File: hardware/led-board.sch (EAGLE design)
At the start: 22 parts, among them U1 ATMEGA168PA-AU

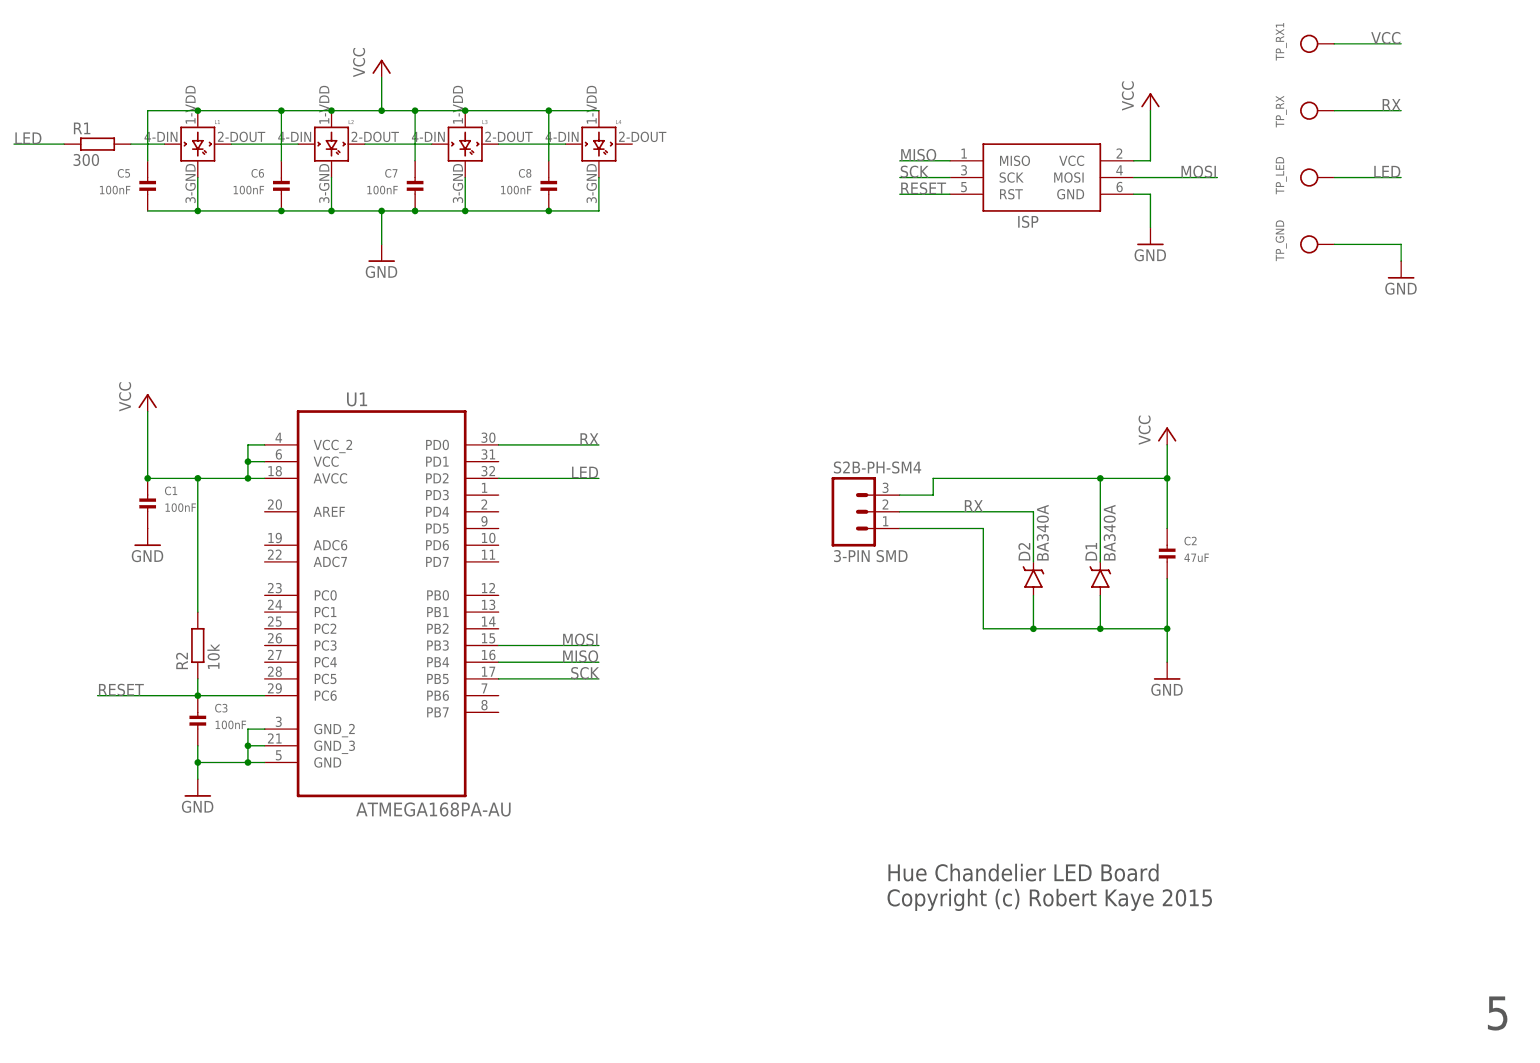
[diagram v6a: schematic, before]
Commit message: Changed L# -> D# for the LEDs
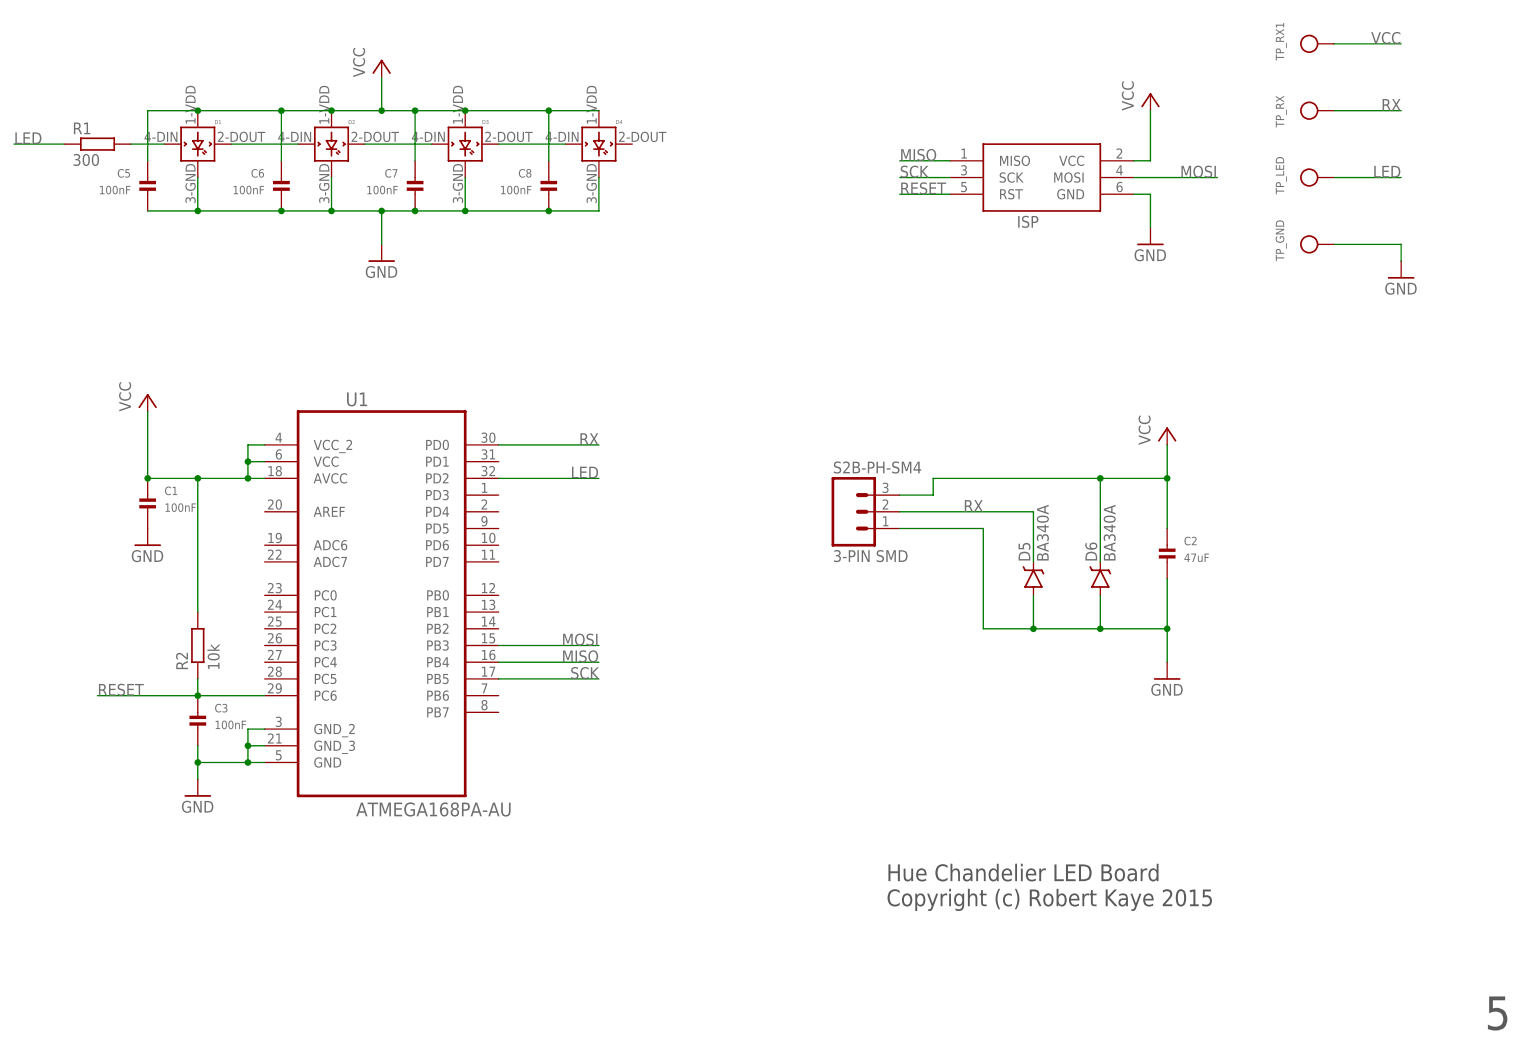
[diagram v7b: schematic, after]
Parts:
- removed L1, L2: WS2812B, adafruit:WS2812B
- added D5, D6: BA340A, SparkFun-DiscreteSemi:B340A
- D1, D2: value BA340A -> WS2812B; device SparkFun-DiscreteSemi:B340A -> adafruit:WS2812B; MPN B330A-13-F -> WS2812B; OC_NEWARK 12T1463 -> 43Y4720
- renumbered L3 to D3, L4 to D4
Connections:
- removed net N$5: D3.DIN, L2.DOUT
- new net D3: D2.DOUT, D3.DIN
- net GND: now also D1.GND, D2.GND, D5.A, D6.A; no longer D1.A, D2.A, L1.GND, L2.GND
- net N$2: now also D1.DOUT, D2.DIN; no longer L1.DOUT, L2.DIN
- net N$8: now also D1.DIN; no longer L1.DIN
- net RX: now also D5.C; no longer D2.C
- net VCC: now also D1.VDD, D2.VDD, D6.C; no longer D1.C, L1.VDD, L2.VDD
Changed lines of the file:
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@@
 </classes>
 <parts>
-<part name="L1" library="adafruit" deviceset="WS2812B" device="">
+<part name="D1" library="adafruit" deviceset="WS2812B" device="">
 <attribute name="MF" value=""/>
 <attribute name="MPN" value="WS2812B"/>
 <attribute name="OC_NEWARK" value="43Y4720"/>
 </part>
-<part name="L2" library="adafruit" deviceset="WS2812B" device="">
+<part name="D2" library="adafruit" deviceset="WS2812B" device="">
 <attribute name="MF" value=""/>
 <attribute name="MPN" value="WS2812B"/>
@@
 <attribute name="OC_NEWARK" value="68T2717"/>
 </part>
-<part name="L3" library="adafruit" deviceset="WS2812B" device="">
+<part name="D3" library="adafruit" deviceset="WS2812B" device="">
 <attribute name="MF" value=""/>
 <attribute name="MPN" value="WS2812B"/>
 <attribute name="OC_NEWARK" value="43Y4720"/>
 </part>
-<part name="L4" library="adafruit" deviceset="WS2812B" device="">
+<part name="D4" library="adafruit" deviceset="WS2812B" device="">
 <attribute name="MF" value=""/>
 <attribute name="MPN" value="WS2812B"/>
@@
 <attribute name="OC_NEWARK" value="68R4880"/>
 </part>
-<part name="D1" library="SparkFun-DiscreteSemi" deviceset="B340A" device="" value="BA340A">
+<part name="D6" library="SparkFun-DiscreteSemi" deviceset="B340A" device="" value="BA340A">
 <attribute name="MF" value=""/>
 <attribute name="MPN" value="B330A-13-F"/>
@@
 <attribute name="OC_NEWARK" value="unknown"/>
 </part>
-<part name="D2" library="SparkFun-DiscreteSemi" deviceset="B340A" device="" value="BA340A">
+<part name="D5" library="SparkFun-DiscreteSemi" deviceset="B340A" device="" value="BA340A">
 <attribute name="MF" value=""/>
 <attribute name="MPN" value="B330A-13-F"/>
@@
 </plain>
 <instances>
-<instance part="L1" gate="G$1" x="-38.1" y="93.98">
+<instance part="D1" gate="G$1" x="-38.1" y="93.98">
 <attribute name="OC_NEWARK" x="-38.1" y="93.98" size="1.778" layer="96" rot="MR0" display="off"/>
 <attribute name="MF" x="-38.1" y="93.98" size="1.778" layer="96" rot="MR0" display="off"/>
 <attribute name="MPN" x="-38.1" y="93.98" size="1.778" layer="96" rot="MR0" display="off"/>
 </instance>
-<instance part="L2" gate="G$1" x="-17.78" y="93.98">
+<instance part="D2" gate="G$1" x="-17.78" y="93.98">
 <attribute name="OC_NEWARK" x="-17.78" y="93.98" size="1.778" layer="96" rot="MR0" display="off"/>
 <attribute name="MF" x="-17.78" y="93.98" size="1.778" layer="96" rot="MR0" display="off"/>
@@
 <attribute name="MF" x="-10.16" y="27.94" size="1.778" layer="96" rot="MR0" display="off"/>
 </instance>
-<instance part="L3" gate="G$1" x="2.54" y="93.98">
+<instance part="D3" gate="G$1" x="2.54" y="93.98">
 <attribute name="OC_NEWARK" x="2.54" y="93.98" size="1.778" layer="96" rot="MR0" display="off"/>
 <attribute name="MF" x="2.54" y="93.98" size="1.778" layer="96" rot="MR0" display="off"/>
 <attribute name="MPN" x="2.54" y="93.98" size="1.778" layer="96" rot="MR0" display="off"/>
 </instance>
-<instance part="L4" gate="G$1" x="22.86" y="93.98">
+<instance part="D4" gate="G$1" x="22.86" y="93.98">
 <attribute name="OC_NEWARK" x="22.86" y="93.98" size="1.778" layer="96" rot="MR0" display="off"/>
 <attribute name="MF" x="22.86" y="93.98" size="1.778" layer="96" rot="MR0" display="off"/>
@@
 <attribute name="MPN" x="109.22" y="30.48" size="1.778" layer="96" rot="MR0" display="off"/>
 </instance>
-<instance part="D1" gate="G$1" x="99.06" y="27.94" rot="R90">
+<instance part="D6" gate="G$1" x="99.06" y="27.94" rot="R90">
 <attribute name="OC_NEWARK" x="99.06" y="27.94" size="1.778" layer="96" rot="MR0" display="off"/>
 <attribute name="MF" x="99.06" y="27.94" size="1.778" layer="96" rot="MR0" display="off"/>
@@
 <attribute name="MPN" x="134.62" y="99.06" size="1.778" layer="96" rot="MR0" display="off"/>
 </instance>
-<instance part="D2" gate="G$1" x="88.9" y="27.94" rot="R90">
+<instance part="D5" gate="G$1" x="88.9" y="27.94" rot="R90">
 <attribute name="OC_NEWARK" x="88.9" y="27.94" size="1.778" layer="96" rot="MR0" display="off"/>
 <attribute name="MF" x="88.9" y="27.94" size="1.778" layer="96" rot="MR0" display="off"/>
@@
 <wire x1="2.54" y1="83.82" x2="15.24" y2="83.82" width="0.1524" layer="91"/>
 <wire x1="15.24" y1="83.82" x2="22.86" y2="83.82" width="0.1524" layer="91"/>
-<pinref part="L4" gate="G$1" pin="GND"/>
+<pinref part="D4" gate="G$1" pin="GND"/>
 <wire x1="22.86" y1="88.9" x2="22.86" y2="83.82" width="0.1524" layer="91"/>
-<pinref part="L3" gate="G$1" pin="GND"/>
+<pinref part="D3" gate="G$1" pin="GND"/>
 <wire x1="2.54" y1="88.9" x2="2.54" y2="83.82" width="0.1524" layer="91"/>
-<pinref part="L2" gate="G$1" pin="GND"/>
+<pinref part="D2" gate="G$1" pin="GND"/>
 <wire x1="-17.78" y1="88.9" x2="-17.78" y2="83.82" width="0.1524" layer="91"/>
-<pinref part="L1" gate="G$1" pin="GND"/>
+<pinref part="D1" gate="G$1" pin="GND"/>
 <wire x1="-38.1" y1="88.9" x2="-38.1" y2="83.82" width="0.1524" layer="91"/>
 <junction x="-38.1" y="83.82"/>
@@
 <wire x1="109.22" y1="20.32" x2="109.22" y2="15.24" width="0.1524" layer="91"/>
 <junction x="109.22" y="20.32"/>
-<pinref part="D2" gate="G$1" pin="A"/>
+<pinref part="D5" gate="G$1" pin="A"/>
 <wire x1="88.9" y1="25.4" x2="88.9" y2="20.32" width="0.1524" layer="91"/>
-<pinref part="D1" gate="G$1" pin="A"/>
+<pinref part="D6" gate="G$1" pin="A"/>
 <wire x1="99.06" y1="25.4" x2="99.06" y2="20.32" width="0.1524" layer="91"/>
 <junction x="99.06" y="20.32"/>
@@
 <net name="N$2" class="0">
 <segment>
-<pinref part="L1" gate="G$1" pin="DOUT"/>
-<pinref part="L2" gate="G$1" pin="DIN"/>
+<pinref part="D1" gate="G$1" pin="DOUT"/>
+<pinref part="D2" gate="G$1" pin="DIN"/>
 <wire x1="-33.02" y1="93.98" x2="-22.86" y2="93.98" width="0.1524" layer="91"/>
 </segment>
@@
 <net name="N$1" class="0">
 <segment>
-<pinref part="L3" gate="G$1" pin="DOUT"/>
-<pinref part="L4" gate="G$1" pin="DIN"/>
+<pinref part="D3" gate="G$1" pin="DOUT"/>
+<pinref part="D4" gate="G$1" pin="DIN"/>
 <wire x1="7.62" y1="93.98" x2="17.78" y2="93.98" width="0.1524" layer="91"/>
 </segment>
@@
 </segment>
 </net>
-<net name="N$5" class="0">
-<segment>
-<pinref part="L2" gate="G$1" pin="DOUT"/>
-<pinref part="L3" gate="G$1" pin="DIN"/>
+<net name="D3" class="0">
+<segment>
+<pinref part="D2" gate="G$1" pin="DOUT"/>
+<pinref part="D3" gate="G$1" pin="DIN"/>
 <wire x1="-12.7" y1="93.98" x2="-2.54" y2="93.98" width="0.1524" layer="91"/>
 </segment>
@@
 <segment>
 <pinref part="R1" gate="G$1" pin="2"/>
-<pinref part="L1" gate="G$1" pin="DIN"/>
+<pinref part="D1" gate="G$1" pin="DIN"/>
 <wire x1="-48.26" y1="93.98" x2="-43.18" y2="93.98" width="0.1524" layer="91"/>
 </segment>
@@
 <segment>
 <wire x1="-45.72" y1="91.44" x2="-45.72" y2="99.06" width="0.1524" layer="91"/>
-<pinref part="L1" gate="G$1" pin="VDD"/>
+<pinref part="D1" gate="G$1" pin="VDD"/>
 <wire x1="-45.72" y1="99.06" x2="-38.1" y2="99.06" width="0.1524" layer="91"/>
-<pinref part="L2" gate="G$1" pin="VDD"/>
+<pinref part="D2" gate="G$1" pin="VDD"/>
 <wire x1="-38.1" y1="99.06" x2="-25.4" y2="99.06" width="0.1524" layer="91"/>
-<pinref part="L3" gate="G$1" pin="VDD"/>
+<pinref part="D3" gate="G$1" pin="VDD"/>
 <wire x1="-25.4" y1="99.06" x2="-17.78" y2="99.06" width="0.1524" layer="91"/>
 <wire x1="-17.78" y1="99.06" x2="-10.16" y2="99.06" width="0.1524" layer="91"/>
-<pinref part="L4" gate="G$1" pin="VDD"/>
+<pinref part="D4" gate="G$1" pin="VDD"/>
 <wire x1="-10.16" y1="99.06" x2="-5.08" y2="99.06" width="0.1524" layer="91"/>
 <wire x1="-5.08" y1="99.06" x2="2.54" y2="99.06" width="0.1524" layer="91"/>
@@
 <wire x1="109.22" y1="43.18" x2="109.22" y2="48.26" width="0.1524" layer="91"/>
 <junction x="109.22" y="43.18"/>
-<pinref part="D1" gate="G$1" pin="C"/>
+<pinref part="D6" gate="G$1" pin="C"/>
 <wire x1="99.06" y1="30.48" x2="99.06" y2="43.18" width="0.1524" layer="91"/>
 <junction x="99.06" y="43.18"/>
@@
 <wire x1="68.58" y1="38.1" x2="88.9" y2="38.1" width="0.1524" layer="91"/>
 <label x="81.28" y="38.1" size="1.778" layer="95" rot="MR0"/>
-<pinref part="D2" gate="G$1" pin="C"/>
+<pinref part="D5" gate="G$1" pin="C"/>
 <wire x1="88.9" y1="38.1" x2="88.9" y2="30.48" width="0.1524" layer="91"/>
 </segment>

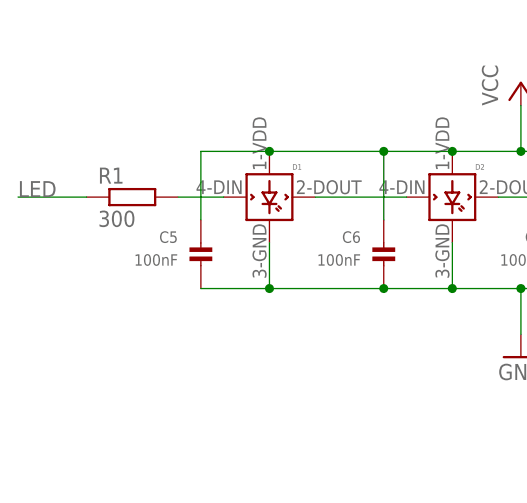
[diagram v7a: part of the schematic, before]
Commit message: Ported code to aduino and it looks like everything should fit!!!
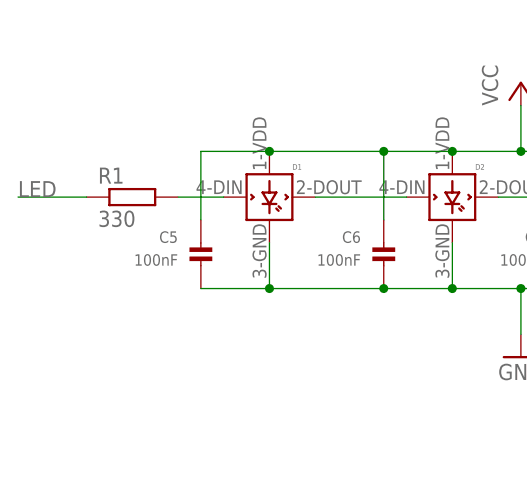
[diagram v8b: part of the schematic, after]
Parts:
- R1: value 300 -> 330; MF Multicomp Passives -> (none); MPN MC01W08051300R -> RC0805JR-07330RL; OC_NEWARK 58K4799 -> 66R3661
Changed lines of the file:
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@@
 <attribute name="OC_NEWARK" value="43Y4720"/>
 </part>
-<part name="R1" library="resistor" deviceset="R-EU_" device="R0805" value="300">
-<attribute name="MF" value="Multicomp Passives"/>
-<attribute name="MPN" value="MC01W08051300R"/>
-<attribute name="OC_NEWARK" value="58K4799"/>
+<part name="R1" library="resistor" deviceset="R-EU_" device="R0805" value="330">
+<attribute name="MF" value=""/>
+<attribute name="MPN" value="RC0805JR-07330RL"/>
+<attribute name="OC_NEWARK" value="66R3661"/>
 </part>
 <part name="S2B-PH-SM4" library="SparkFun-Connectors" deviceset="M03" device="JST-SMD" value="3-PIN SMD">
